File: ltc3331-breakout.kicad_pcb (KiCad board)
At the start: 2 copper layers, 100 x 100 mm, 75 parts, among them IC1 LTC3331, J1 CONN_01X04, J10 CONN_01X02_FEMALE, J11 CONN_01X04, J12 CONN_01X03, J13 CONN_01X03, J14 CONN_01X03, J15 CONN_02X12, J16 CONN_02X08, J17 CONN_02X08, J18 CONN_02X08, J19 CONN_02X08, J2 CONN_01X03, J20 CONN_02X04, J3 CONN_01X03, J4 CONN_01X03, J5 CONN_01X02, J6 CONN_01X04, J7 CONN_01X03, J8 CONN_01X03, J9 CONN_01X03, U1 NC7SZ58, U2 NC7SZ58

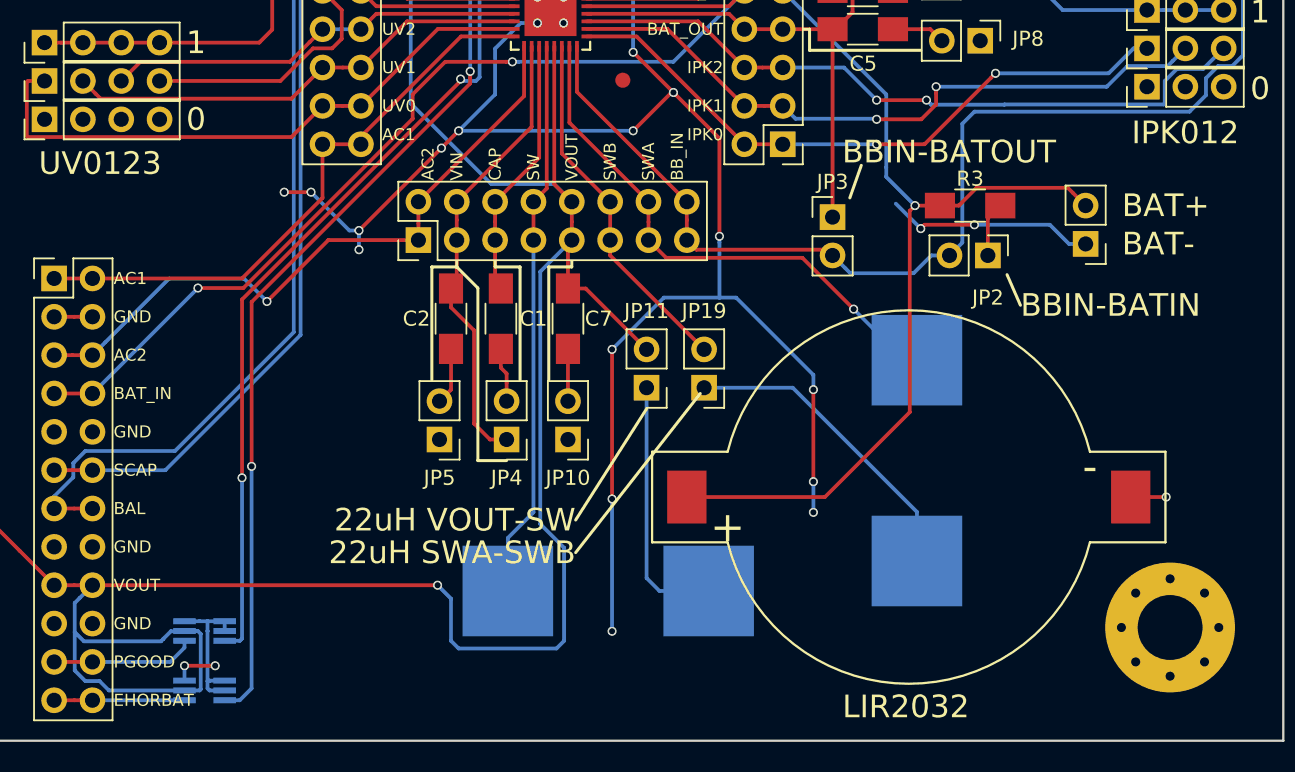
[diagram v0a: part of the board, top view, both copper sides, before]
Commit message: replace 22uF inductor footprints with better ones
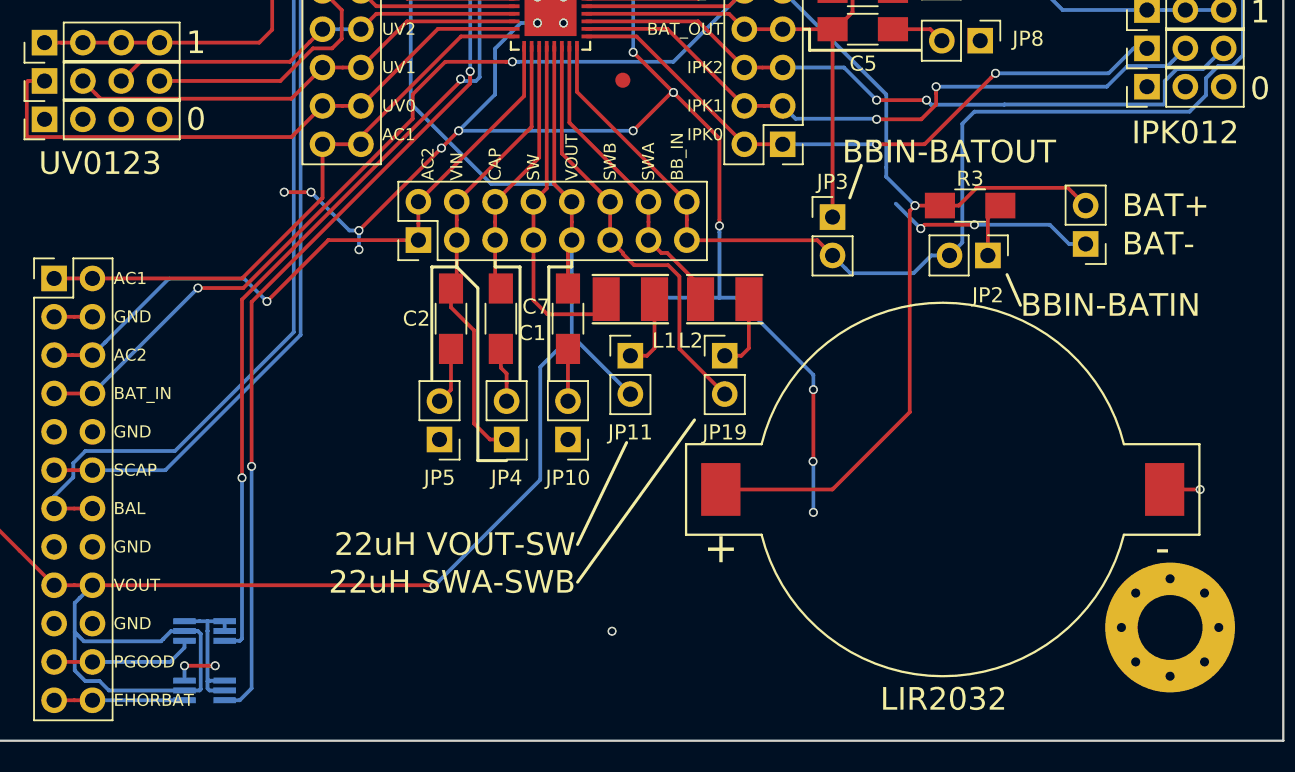
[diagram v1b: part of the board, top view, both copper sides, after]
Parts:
- L1, L2: footprint Inductors:Inductor_Wurth_HCI-1890 -> Inductors:Inductor_Taiyo-Yuden_NR-30xx_HandSoldering; moved to F.Cu
- moved L1 19.4 mm to (106.8, 120.8)
- moved L2 16.6 mm to (113.0, 120.8), turned to 0 degrees
- moved JP19 2.52 mm to (113.0, 124.5), turned to 0 degrees
- moved JP11 2.38 mm to (106.8, 124.5), turned to 0 degrees
- moved BT1 2.30 mm to (127.4, 133.4)
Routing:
- net GND: track 229.9 -> 206.4 mm, vias 39 -> 36
- net Net-(JP19-Pad1): track 20.8 -> 5.06 mm
- net /SWA: track 36.1 -> 20.6 mm, vias 1 -> 0
- net /VOUT: track 299.4 -> 284.4 mm
- net /SW: track 37.1 -> 23.1 mm
- net Net-(JP11-Pad1): track 17.1 -> 5.06 mm
- net /SWB: track 24.0 -> 28.8 mm
- net /BAT_IN: track 155.1 -> 152.6 mm
- net (no net): vias 2 -> 3

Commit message: move U1,U2 to front side to clear rear side of all required components.
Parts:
- U1, U2: moved to F.Cu
- moved U1 2.23 mm to (80.7, 143.3)
- moved U2 2.16 mm to (80.7, 146.8)
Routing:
- net /VOUT: track 284.4 -> 269.8 mm, vias 4 -> 6
- net /EHORBAT: track 8.64 -> 11.3 mm
- net /PGOOD: track 9.48 -> 11.7 mm
- net /EH_ON: track 80.7 -> 78.6 mm, vias 2 -> 3
- net /PGVOUT: track 78.7 -> 76.8 mm, vias 2 -> 3
- net GND: track 206.4 -> 207.7 mm, vias 36 -> 34

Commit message: routed changes
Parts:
- removed FID** (x8): fiducial_i.5mm_o1.5mm, footprints:fiducial_i.5mm_o1.5mm
- removed REF** (x4): MountingHole_4.3mm_M4_Pad_Via, Mounting_Holes:MountingHole_4.3mm_M4_Pad_Via
- removed REF**: KiCAD Logo, Symbols:Symbol_KiCAD-Logo_CopperAndSilkScreenTop
- removed REF***: OSHW-Logo2_14.6x12mm_SilkScreen, Symbols:OSHW-Logo2_14.6x12mm_SilkScreen
- added D1: CMOSH-3, Diodes_SMD:D_SOD-523, F.Cu at (137.4, 70.1)
- added J19: Conn_02x02_Odd_Even, Pin_Headers:Pin_Header_Straight_2x02_Pitch2.54mm, F.Cu at (55.9, 100.7)
- added J21: Conn_02x02_Odd_Even, Pin_Headers:Pin_Header_Straight_2x02_Pitch2.54mm, F.Cu at (54.3, 143.1)
- added J22: Conn_02x02_Odd_Even, Pin_Headers:Pin_Header_Straight_2x02_Pitch2.54mm, F.Cu at (54.6, 54.6)
- added J23: Conn_02x02_Odd_Even, Pin_Headers:Pin_Header_Straight_2x02_Pitch2.54mm, F.Cu at (143.3, 142.7)
- added JP17: Jumper, Pin_Headers:Pin_Header_Straight_1x02_Pitch2.54mm, F.Cu at (144.0, 82.3)
- added JP21: Jumper, Pin_Headers:Pin_Header_Straight_1x02_Pitch2.54mm, F.Cu at (141.5, 79.8)
- added Q1: NDC7001C, TO_SOT_Packages_SMD:SuperSOT-6, F.Cu at (141.3, 70.9)
- added Q2: CMPT3906E, TO_SOT_Packages_SMD:SOT-23, F.Cu at (144.1, 66.1)
- added R4: 100K, Resistors_SMD:R_1206_HandSoldering, F.Cu at (137.2, 74.4)
- added R5: 1M, Resistors_SMD:R_1206_HandSoldering, F.Cu at (140.4, 65.1)
- added R6: 56.2, Resistors_SMD:R_1206_HandSoldering, F.Cu at (137.4, 65.1)
- J20: value CONN_02X04 -> Conn_02x02_Odd_Even; footprint Pin_Headers:Pin_Header_Straight_2x04_Pitch2.54mm -> Pin_Headers:Pin_Header_Straight_2x02_Pitch2.54mm
- R2: renamed from R3; value 100 -> 1M
- moved J20 105.5 mm to (142.4, 55.1)
- moved BT1 71.3 mm to (118.9, 62.6), turned to 180 degrees
- moved J17 63.6 mm to (133.1, 53.6), turned to 0 degrees
- moved R2 43.9 mm to (145.1, 73.6), turned to 270 degrees
- moved JP16 36.6 mm to (138.9, 82.3), turned to 180 degrees
- moved J10 11.2 mm to (146.0, 114.1), turned to 270 degrees
- moved J14 11.2 mm to (146.0, 111.6), turned to 270 degrees
- moved J6 11.2 mm to (146.0, 116.7), turned to 270 degrees
- moved J13 7.06 mm to (75.0, 103.8), turned to 270 degrees
- moved J5 7.06 mm to (75.0, 108.8), turned to 270 degrees
- moved J9 7.06 mm to (75.0, 106.3), turned to 270 degrees
- moved J11 5.00 mm to (146.0, 94.0), turned to 270 degrees
- moved J12 5.00 mm to (100.6, 75.4), turned to 270 degrees
- moved J15 5.00 mm to (146.0, 91.4), turned to 270 degrees
- moved J16 5.00 mm to (100.6, 72.9), turned to 270 degrees
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- renumbered J16 to J1, J7 to J10, J8 to J11, J9 to J12, J11 to J13, J12 to J14, J13 to J15, J14 to J16, J5 to J17, J10 to J18, J17 to J2, J15 to J24, J18 to J3, J19 to J4, J1 to J5, J2 to J6, J3 to J7, J4 to J8, J6 to J9, JP11 to JP1, JP12 to JP10, JP13 to JP11, JP14 to JP12, JP16 to JP13, JP17 to JP14, JP18 to JP15, JP2 to JP16, JP1 to JP18, JP3 to JP19, JP4 to JP2, JP15 to JP20, JP5 to JP3, JP6 to JP4, JP7 to JP5, JP8 to JP6, JP9 to JP7, JP10 to JP8, JP19 to JP9, R2 to R3
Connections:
- JP16 pad 1: Net-(JP2-Pad1) -> /CHARGE
- JP16 pad 2: /BB_IN -> Net-(JP16-Pad2)
- R2 pad 1: /BAT_IN -> Net-(JP16-Pad2)
- R2 pad 2: Net-(JP2-Pad1) -> GND
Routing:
- net /VIN: track 30.4 -> 74.1 mm, vias 0 -> 2
- net /AC2: track 44.3 -> 70.8 mm, vias 1 -> 2
- net Net-(JP17-Pad2): track 0.00 -> 26.1 mm
- net /AC1: track 39.5 -> 64.2 mm, vias 0 -> 1
- net /BAT_IN: track 152.6 -> 135.9 mm, vias 3 -> 4
- net GND: track 207.7 -> 191.8 mm, vias 34 -> 28
- net Net-(JP16-Pad2): track 0.00 -> 15.9 mm, vias 0 -> 1
- net Net-(Q1-Pad3): track 0.00 -> 15.7 mm, vias 0 -> 2
- net Net-(D1-Pad1): track 0.00 -> 14.4 mm, vias 0 -> 1
- net /CHARGE: track 40.4 -> 54.6 mm, vias 0 -> 1
- net /UV0: track 40.1 -> 26.9 mm
- net Net-(Q1-Pad2): track 0.00 -> 10.5 mm
- net /VIN3: track 82.5 -> 89.8 mm, vias 0 -> 1
- net /FLOAT0: track 40.6 -> 47.6 mm
- net /IPK0: track 42.7 -> 49.6 mm, vias 2 -> 1
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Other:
- board text added: "BAT- BAT+"
- board text added: "BATOUT BBIN"
- board text added: "ChargeR"
- board text added: "FastCharge"
- board text added: "IPK210"
- board text added: "LBSELFLOAT10"
- board text added: "LTC3331 breakout board v0.2 2018 by David R. Piegdon github.com/dpiegdon/ltc3331-breakout"
- board text added: "OUT210"
- board text added: "UV03210"
- board text removed: "BAT+"
- board text removed: "BAT-"
- board text removed: "BBIN-BATIN"
- board text removed: "BBIN-BATOUT"
- board text removed: "CHARGE CURRENT RESISTOR"
- board text removed: "FLOAT01LBSEL"
- board text removed: "IPK012"
- board text removed: "LTC3331 breakout board v0.1 2017 by David R. Piegdon github.com/dpiegdon/ltc3331-breakout"
- board text removed: "OUT012"
- board text removed: "UV0123"

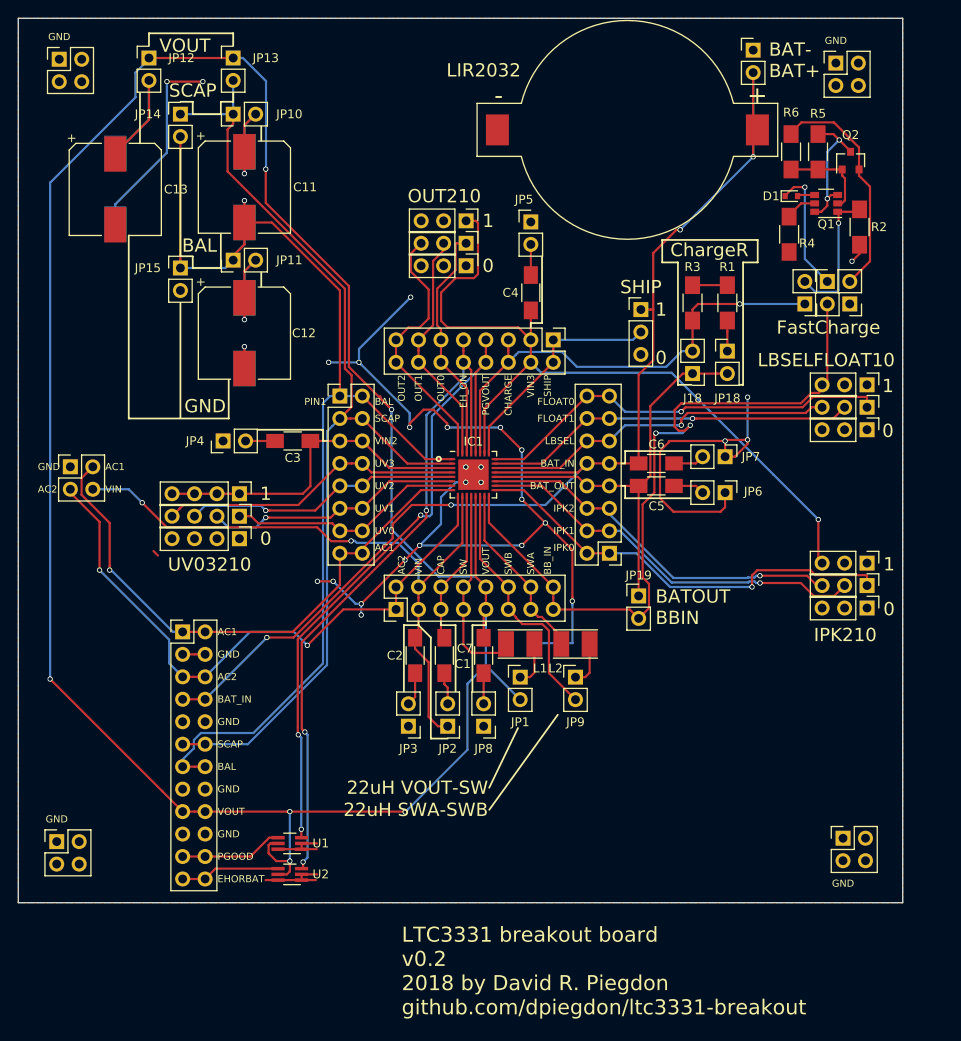
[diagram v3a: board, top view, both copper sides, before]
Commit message: replaced some capacitors with generic footprint, rerouted
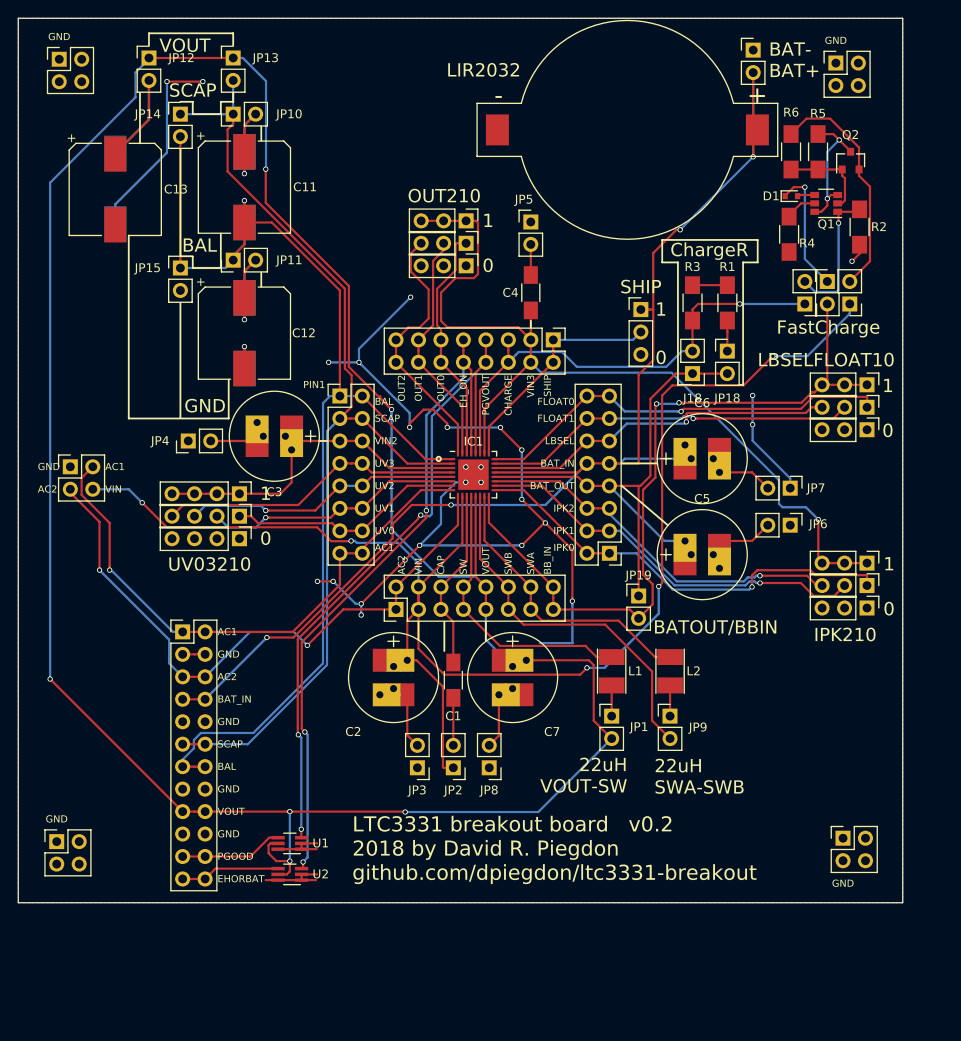
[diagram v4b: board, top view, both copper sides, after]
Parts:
- C2, C3, C5, C6, C7: footprint Capacitors_SMD:C_1206_HandSoldering -> footprints:CAP_Generic_SMD_Radial_D10.0mm_P2.50mm_P5.00mm
- moved JP9 11.6 mm to (123.7, 128.9)
- moved JP1 11.2 mm to (117.1, 128.9)
- moved L2 11.1 mm to (123.7, 123.8), turned to 270 degrees
- moved L1 10.8 mm to (117.1, 123.8), turned to 270 degrees
- moved C5 8.72 mm to (126.1, 110.6)
- moved JP6 8.24 mm to (137.3, 107.3)
- moved JP7 8.18 mm to (137.3, 103.1)
- moved JP3 4.81 mm to (95.1, 134.7)
- moved JP8 4.74 mm to (103.3, 134.7)
- moved JP2 4.74 mm to (99.2, 134.7)
- moved C6 3.98 mm to (126.1, 99.8)
- moved JP4 3.94 mm to (69.2, 97.8)
- moved C7 3.50 mm to (105.9, 123.3)
- moved C1 2.97 mm to (99.2, 124.8)
- moved C2 2.74 mm to (92.4, 123.3)
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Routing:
- net /VIN: track 74.1 -> 172.6 mm, vias 2 -> 5
- net GND: track 191.8 -> 168.1 mm, vias 28 -> 27
- net /VOUT: track 269.8 -> 288.7 mm
- net /BAT_OUT: track 49.1 -> 64.3 mm
- net /SWB: track 28.8 -> 41.8 mm
- net /BAT_IN: track 135.9 -> 148.7 mm
- net /SWA: track 20.6 -> 33.0 mm
- net /VIN3: track 89.8 -> 101.5 mm
- net /SW: track 23.1 -> 32.2 mm
- net Net-(C3-Pad2): track 3.33 -> 9.85 mm
- net Net-(C7-Pad2): track 3.46 -> 9.85 mm
- net Net-(C6-Pad2): track 3.55 -> 9.88 mm
- net Net-(C5-Pad2): track 3.55 -> 9.88 mm
- net Net-(C2-Pad2): track 3.78 -> 9.87 mm
- net /VIN2: track 38.4 -> 41.8 mm
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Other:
- board text added: "BATOUT/BBIN"
- board text removed: "BATOUT BBIN"
